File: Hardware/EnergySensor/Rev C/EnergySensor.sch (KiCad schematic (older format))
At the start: 40 parts, among them IC1 ATMEGA328P-A, J1 JACK_3POLE, P1 MAINS, P2 CONN_02X03, P3 CONN_01X12, T1 VN20.10 09477, U1 LM1084IT-3.3/NOPB, Y1 16MHz

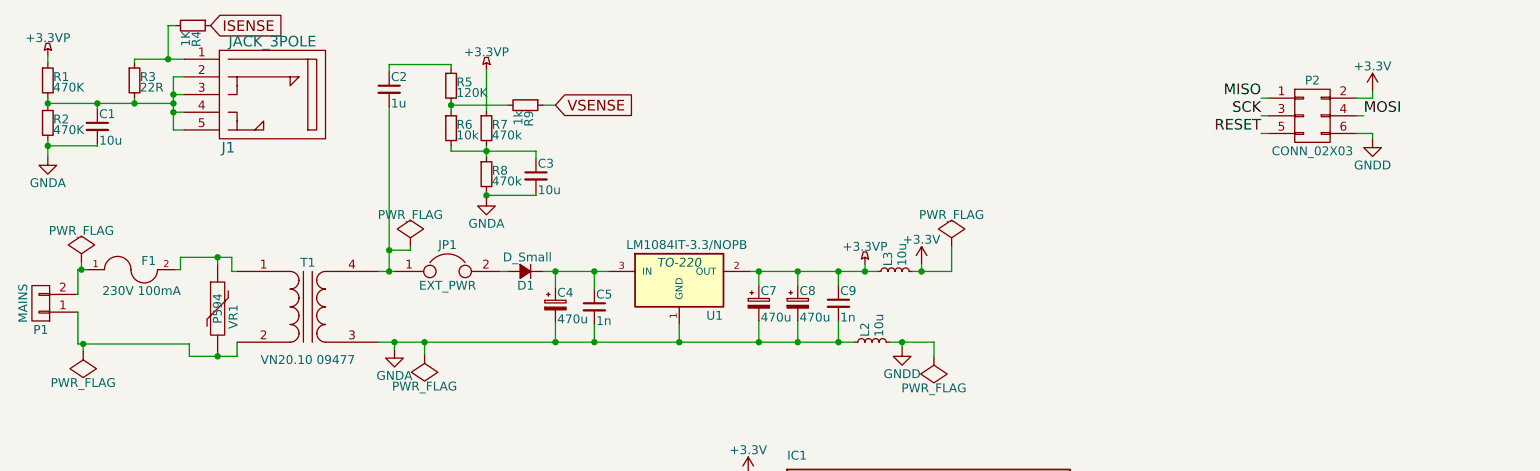
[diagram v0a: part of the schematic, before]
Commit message: moved energy sensor to nice case and various tweaks
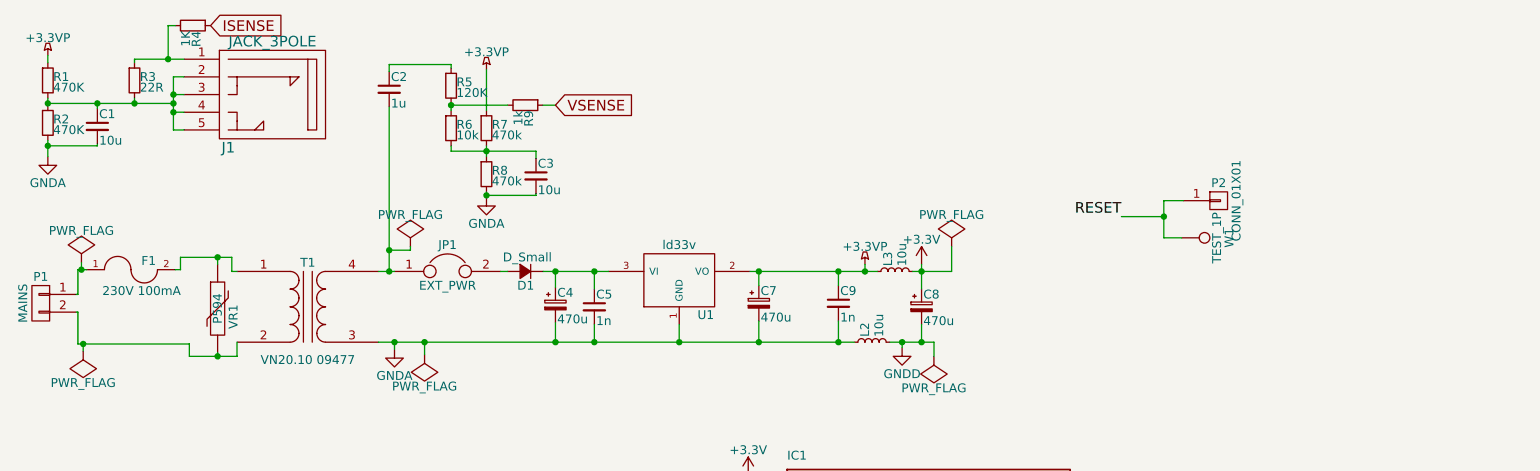
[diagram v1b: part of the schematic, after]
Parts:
- removed P2: CONN_02X03, Pin_Headers:Pin_Header_Straight_2x03, symbol CONN_02X03
- removed U1: LM1084IT-3.3/NOPB, TO-220, symbol LM1084IT-3.3/NOPB
- added P2: CONN_01X01, Pin_Headers:Pin_Header_Straight_1x01, symbol CONN_01X01
- added U1: ld33v, TO_SOT_Packages_THT:TO-220_Neutral123_Vertical, symbol ld33v
- added W1: TEST_1P, Measurement_Points:Measurement_Point_Round-SMD-Pad_Big, symbol TEST_1P
- L1, L2, L3: footprint Inductors:NR4018_HandSoldering -> Inductors:Inductor_1212
- P3: footprint Pin_Headers:Pin_Header_Angled_1x12 -> Socket_Strips:Socket_Strip_Angled_1x12
- T1: footprint Divers:TEZ-22x24 -> CustomParts:TEZ-22x24
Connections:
- net +3.3VP: now also U1.2 (VO); no longer C8.1
- net +3V3: now also C8.1
- net GNDA: now also U1.1 (GND); no longer C8.2
- net GNDD: now also C8.2
- net RESET: now also P2.1 (P1), W1.1
- net at F1.1: now also P1.1 (P1); no longer P1.2 (P2)
- net at T1.2 (AB), VR1.2: now also P1.2 (P2); no longer P1.1 (P1)
- net at C4.1, C5.1, D1.1 (K): now also U1.3 (VI)
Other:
- moved on the sheet: C8
